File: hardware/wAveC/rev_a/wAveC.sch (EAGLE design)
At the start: 2 parts

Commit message: added some layout
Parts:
- added J1, J2: WIRE_HOLE-14AWG, ac:WIRE_HOLE-14AWG
- R1: value (none) -> 160; DIGIKEY (none) -> P160QCT-ND
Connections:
- new net CURRENT: CT1.1, R1.2
- new net GND: CT1.2, R1.1
- new net PHASE: J1.P$1, J2.P$1
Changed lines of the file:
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@@
 <setting verticaltext="up"/>
 </settings>
-<grid distance="0.1" unitdist="inch" unit="inch" style="lines" multiple="1" display="no" altdistance="0.01" altunitdist="inch" altunit="inch"/>
+<grid distance="0.1" unitdist="inch" unit="inch" style="lines" multiple="1" display="yes" altdistance="0.01" altunitdist="inch" altunit="inch"/>
 <layers>
 <layer number="1" name="Top" color="4" fill="1" visible="no" active="no"/>
@@
 <part name="FRAME1" library="frames" deviceset="LETTER_L" device=""/>
 <part name="CT1" library="ac" deviceset="CR8348" device="-1000"/>
-<part name="R1" library="rcl" deviceset="R-US_" device="R1210"/>
+<part name="R1" library="rcl" deviceset="R-US_" device="R1210" value="160">
+<attribute name="DIGIKEY" value="P160QCT-ND"/>
+</part>
+<part name="GND1" library="supply1" deviceset="GND" device=""/>
+<part name="J1" library="ac" deviceset="WIRE_HOLE-14AWG" device=""/>
+<part name="J2" library="ac" deviceset="WIRE_HOLE-14AWG" device=""/>
 </parts>
 <sheets>
@@
 <instance part="FRAME1" gate="G$2" x="147.32" y="0"/>
 <instance part="CT1" gate="G$1" x="86.36" y="116.84"/>
-<instance part="R1" gate="G$1" x="104.14" y="116.84" rot="R90"/>
+<instance part="R1" gate="G$1" x="104.14" y="116.84" rot="R90">
+<attribute name="DIGIKEY" x="104.14" y="116.84" size="1.27" layer="96" rot="R90" display="off"/>
+</instance>
+<instance part="GND1" gate="1" x="111.76" y="106.68"/>
+<instance part="J1" gate="G$1" x="88.9" y="162.56" rot="MR0"/>
+<instance part="J2" gate="G$1" x="88.9" y="154.94" rot="MR0"/>
 </instances>
 <busses>
 </busses>
 <nets>
+<net name="CURRENT" class="0">
+<segment>
+<pinref part="CT1" gate="G$1" pin="1"/>
+<wire x1="91.44" y1="121.92" x2="104.14" y2="121.92" width="0.1524" layer="91"/>
+<pinref part="R1" gate="G$1" pin="2"/>
+<wire x1="104.14" y1="121.92" x2="111.76" y2="121.92" width="0.1524" layer="91"/>
+<junction x="104.14" y="121.92"/>
+<label x="111.76" y="121.92" size="1.27" layer="95" xref="yes"/>
+</segment>
+</net>
+<net name="GND" class="0">
+<segment>
+<pinref part="CT1" gate="G$1" pin="2"/>
+<wire x1="91.44" y1="111.76" x2="104.14" y2="111.76" width="0.1524" layer="91"/>
+<wire x1="104.14" y1="111.76" x2="111.76" y2="111.76" width="0.1524" layer="91"/>
+<wire x1="111.76" y1="111.76" x2="111.76" y2="109.22" width="0.1524" layer="91"/>
+<pinref part="GND1" gate="1" pin="GND"/>
+<junction x="111.76" y="109.22"/>
+<pinref part="R1" gate="G$1" pin="1"/>
+<junction x="104.14" y="111.76"/>
+</segment>
+</net>
+<net name="PHASE" class="0">
+<segment>
+<pinref part="J2" gate="G$1" pin="P$1"/>
+<wire x1="86.36" y1="154.94" x2="83.82" y2="154.94" width="0.1524" layer="91"/>
+<label x="83.82" y="154.94" size="1.27" layer="95" rot="R180" xref="yes"/>
+</segment>
+<segment>
+<pinref part="J1" gate="G$1" pin="P$1"/>
+<wire x1="86.36" y1="162.56" x2="83.82" y2="162.56" width="0.1524" layer="91"/>
+<label x="83.82" y="162.56" size="1.27" layer="95" rot="R180" xref="yes"/>
+</segment>
+</net>
 </nets>
 </sheet>

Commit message: wavec routed
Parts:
- added J3, J4: MOLEX_BNC_73100-0105, connector:MOLEX_BNC_73100-0105
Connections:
- net CURRENT: now also J3.SIGNAL
- net GND: now also J3.GND
- net PHASE: now also J4.SIGNAL
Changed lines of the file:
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@@
 <setting verticaltext="up"/>
 </settings>
-<grid distance="0.1" unitdist="inch" unit="inch" style="lines" multiple="1" display="yes" altdistance="0.01" altunitdist="inch" altunit="inch"/>
+<grid distance="0.1" unitdist="inch" unit="inch" style="lines" multiple="1" display="no" altdistance="0.01" altunitdist="inch" altunit="inch"/>
 <layers>
 <layer number="1" name="Top" color="4" fill="1" visible="no" active="no"/>
@@
 <part name="J1" library="ac" deviceset="WIRE_HOLE-14AWG" device=""/>
 <part name="J2" library="ac" deviceset="WIRE_HOLE-14AWG" device=""/>
+<part name="J3" library="connector" deviceset="MOLEX_BNC_73100-0105" device=""/>
+<part name="J4" library="connector" deviceset="MOLEX_BNC_73100-0105" device=""/>
+<part name="GND2" library="supply1" deviceset="GND" device=""/>
 </parts>
 <sheets>
@@
 <instance part="J1" gate="G$1" x="88.9" y="162.56" rot="MR0"/>
 <instance part="J2" gate="G$1" x="88.9" y="154.94" rot="MR0"/>
+<instance part="J3" gate="G$1" x="134.62" y="160.02"/>
+<instance part="J4" gate="G$1" x="134.62" y="144.78"/>
+<instance part="GND2" gate="1" x="144.78" y="149.86"/>
 </instances>
 <busses>
@@
 <junction x="104.14" y="121.92"/>
 <label x="111.76" y="121.92" size="1.27" layer="95" xref="yes"/>
+</segment>
+<segment>
+<pinref part="J3" gate="G$1" pin="SIGNAL"/>
+<wire x1="142.24" y1="160.02" x2="144.78" y2="160.02" width="0.1524" layer="91"/>
+<label x="144.78" y="160.02" size="1.27" layer="95" xref="yes"/>
 </segment>
 </net>
@@
 <junction x="104.14" y="111.76"/>
 </segment>
+<segment>
+<pinref part="J3" gate="G$1" pin="GND"/>
+<wire x1="142.24" y1="154.94" x2="144.78" y2="154.94" width="0.1524" layer="91"/>
+<wire x1="144.78" y1="154.94" x2="144.78" y2="152.4" width="0.1524" layer="91"/>
+<pinref part="GND2" gate="1" pin="GND"/>
+</segment>
 </net>
 <net name="PHASE" class="0">
@@
 <label x="83.82" y="162.56" size="1.27" layer="95" rot="R180" xref="yes"/>
 </segment>
+<segment>
+<pinref part="J4" gate="G$1" pin="SIGNAL"/>
+<wire x1="142.24" y1="144.78" x2="144.78" y2="144.78" width="0.1524" layer="91"/>
+<label x="144.78" y="144.78" size="1.27" layer="95" xref="yes"/>
+</segment>
 </net>

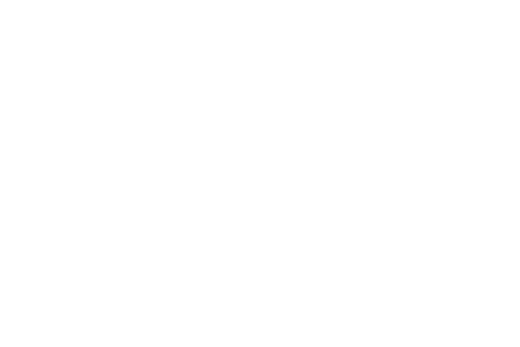
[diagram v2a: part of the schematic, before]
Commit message: added silkscreen
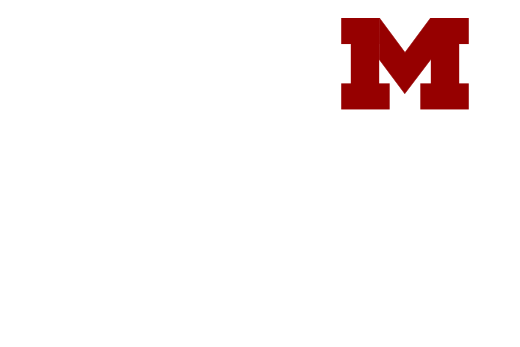
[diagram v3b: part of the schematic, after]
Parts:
- added LOGO1: UMICH_SOLID_MEDIUM, logos:UMICH_SOLID_MEDIUM
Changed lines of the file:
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@@
 <part name="J4" library="connector" deviceset="MOLEX_BNC_73100-0105" device=""/>
 <part name="GND2" library="supply1" deviceset="GND" device=""/>
+<part name="LOGO1" library="logos" deviceset="UMICH_SOLID" device="_MEDIUM"/>
 </parts>
 <sheets>
@@
 <instance part="J4" gate="G$1" x="134.62" y="144.78"/>
 <instance part="GND2" gate="1" x="144.78" y="149.86"/>
+<instance part="LOGO1" gate="G$1" x="231.14" y="172.72"/>
 </instances>
 <busses>

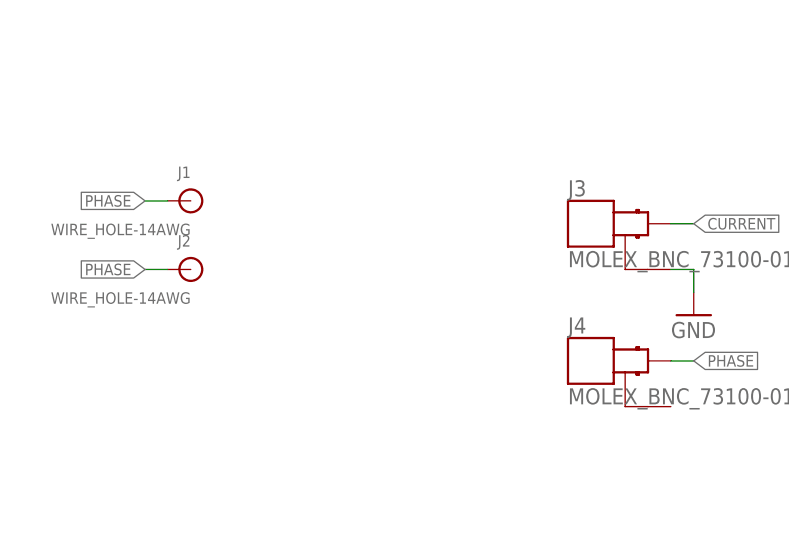
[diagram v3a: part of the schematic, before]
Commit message: updated wavec labels and date
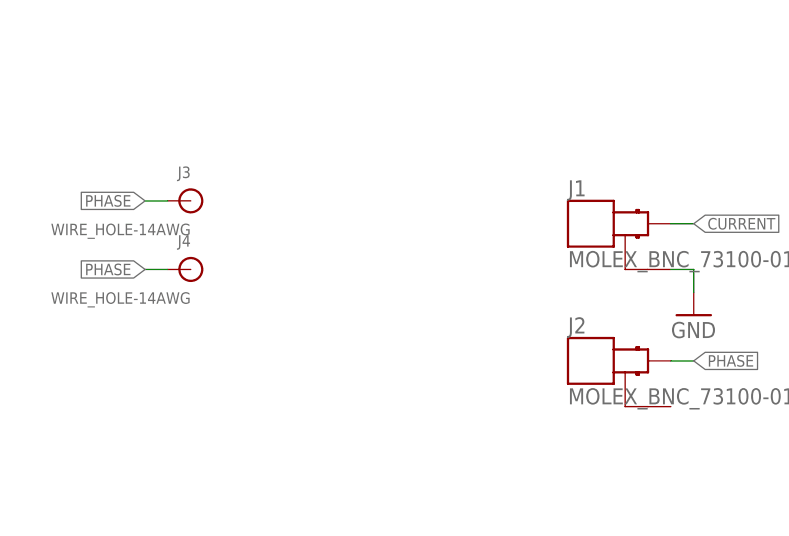
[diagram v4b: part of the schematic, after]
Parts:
- J1, J2: value WIRE_HOLE-14AWG -> MOLEX_BNC_73100-0105; device ac:WIRE_HOLE-14AWG -> connector:MOLEX_BNC_73100-0105
- J3, J4: value MOLEX_BNC_73100-0105 -> WIRE_HOLE-14AWG; device connector:MOLEX_BNC_73100-0105 -> ac:WIRE_HOLE-14AWG
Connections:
- net CURRENT: now also J1.SIGNAL; no longer J3.SIGNAL
- net GND: now also J1.GND; no longer J3.GND
- net PHASE: now also J2.SIGNAL, J3.P$1, J4.P$1; no longer J1.P$1, J2.P$1, J4.SIGNAL
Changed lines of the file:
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@@
 </part>
 <part name="GND1" library="supply1" deviceset="GND" device=""/>
-<part name="J1" library="ac" deviceset="WIRE_HOLE-14AWG" device=""/>
-<part name="J2" library="ac" deviceset="WIRE_HOLE-14AWG" device=""/>
-<part name="J3" library="connector" deviceset="MOLEX_BNC_73100-0105" device=""/>
-<part name="J4" library="connector" deviceset="MOLEX_BNC_73100-0105" device=""/>
+<part name="J3" library="ac" deviceset="WIRE_HOLE-14AWG" device=""/>
+<part name="J4" library="ac" deviceset="WIRE_HOLE-14AWG" device=""/>
+<part name="J1" library="connector" deviceset="MOLEX_BNC_73100-0105" device=""/>
+<part name="J2" library="connector" deviceset="MOLEX_BNC_73100-0105" device=""/>
 <part name="GND2" library="supply1" deviceset="GND" device=""/>
 <part name="LOGO1" library="logos" deviceset="UMICH_SOLID" device="_MEDIUM"/>
@@
 </instance>
 <instance part="GND1" gate="1" x="111.76" y="106.68"/>
-<instance part="J1" gate="G$1" x="88.9" y="162.56" rot="MR0"/>
-<instance part="J2" gate="G$1" x="88.9" y="154.94" rot="MR0"/>
-<instance part="J3" gate="G$1" x="134.62" y="160.02"/>
-<instance part="J4" gate="G$1" x="134.62" y="144.78"/>
+<instance part="J3" gate="G$1" x="88.9" y="162.56" rot="MR0"/>
+<instance part="J4" gate="G$1" x="88.9" y="154.94" rot="MR0"/>
+<instance part="J1" gate="G$1" x="134.62" y="160.02"/>
+<instance part="J2" gate="G$1" x="134.62" y="144.78"/>
 <instance part="GND2" gate="1" x="144.78" y="149.86"/>
 <instance part="LOGO1" gate="G$1" x="231.14" y="172.72"/>
@@
 </segment>
 <segment>
-<pinref part="J3" gate="G$1" pin="SIGNAL"/>
+<pinref part="J1" gate="G$1" pin="SIGNAL"/>
 <wire x1="142.24" y1="160.02" x2="144.78" y2="160.02" width="0.1524" layer="91"/>
 <label x="144.78" y="160.02" size="1.27" layer="95" xref="yes"/>
@@
 </segment>
 <segment>
-<pinref part="J3" gate="G$1" pin="GND"/>
+<pinref part="J1" gate="G$1" pin="GND"/>
 <wire x1="142.24" y1="154.94" x2="144.78" y2="154.94" width="0.1524" layer="91"/>
 <wire x1="144.78" y1="154.94" x2="144.78" y2="152.4" width="0.1524" layer="91"/>
@@
 <net name="PHASE" class="0">
 <segment>
-<pinref part="J2" gate="G$1" pin="P$1"/>
+<pinref part="J4" gate="G$1" pin="P$1"/>
 <wire x1="86.36" y1="154.94" x2="83.82" y2="154.94" width="0.1524" layer="91"/>
 <label x="83.82" y="154.94" size="1.27" layer="95" rot="R180" xref="yes"/>
 </segment>
 <segment>
-<pinref part="J1" gate="G$1" pin="P$1"/>
+<pinref part="J3" gate="G$1" pin="P$1"/>
 <wire x1="86.36" y1="162.56" x2="83.82" y2="162.56" width="0.1524" layer="91"/>
 <label x="83.82" y="162.56" size="1.27" layer="95" rot="R180" xref="yes"/>
 </segment>
 <segment>
-<pinref part="J4" gate="G$1" pin="SIGNAL"/>
+<pinref part="J2" gate="G$1" pin="SIGNAL"/>
 <wire x1="142.24" y1="144.78" x2="144.78" y2="144.78" width="0.1524" layer="91"/>
 <label x="144.78" y="144.78" size="1.27" layer="95" xref="yes"/>
